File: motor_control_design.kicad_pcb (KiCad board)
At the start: 2 copper layers, 57.1 x 57.2 mm, 97 parts, among them J1 TYPE-C-31-M-12, J10 5V, J2 SWD, J3 VBAT, J4 GND, J5 FC_M/P, J6 Conn_01x06, J7 Conn_01x04_Pin, J8 Conn_01x06, J9 GND, Q1 RF1S9540SM, Q10 2N7002, Q11 2N7002, Q12 2N7002, Q13 2N7002, Q14 RF1S9540SM, Q15 IRLZ44NS, Q16 2N7002, Q2 RF1S9540SM, Q3 IRLZ44NS, Q4 2N7002, Q5 2N7002, Q6 RF1S9540SM, Q7 IRLZ44NS, Q8 2N7002, Q9 IRLZ44NS, U1 STM32F401CCU6, U2 LT1962-3.3, U3 LTC4365DDB, U4 TPS563200, U5 SSM6N7002KFU_LF, Y1 16MHz

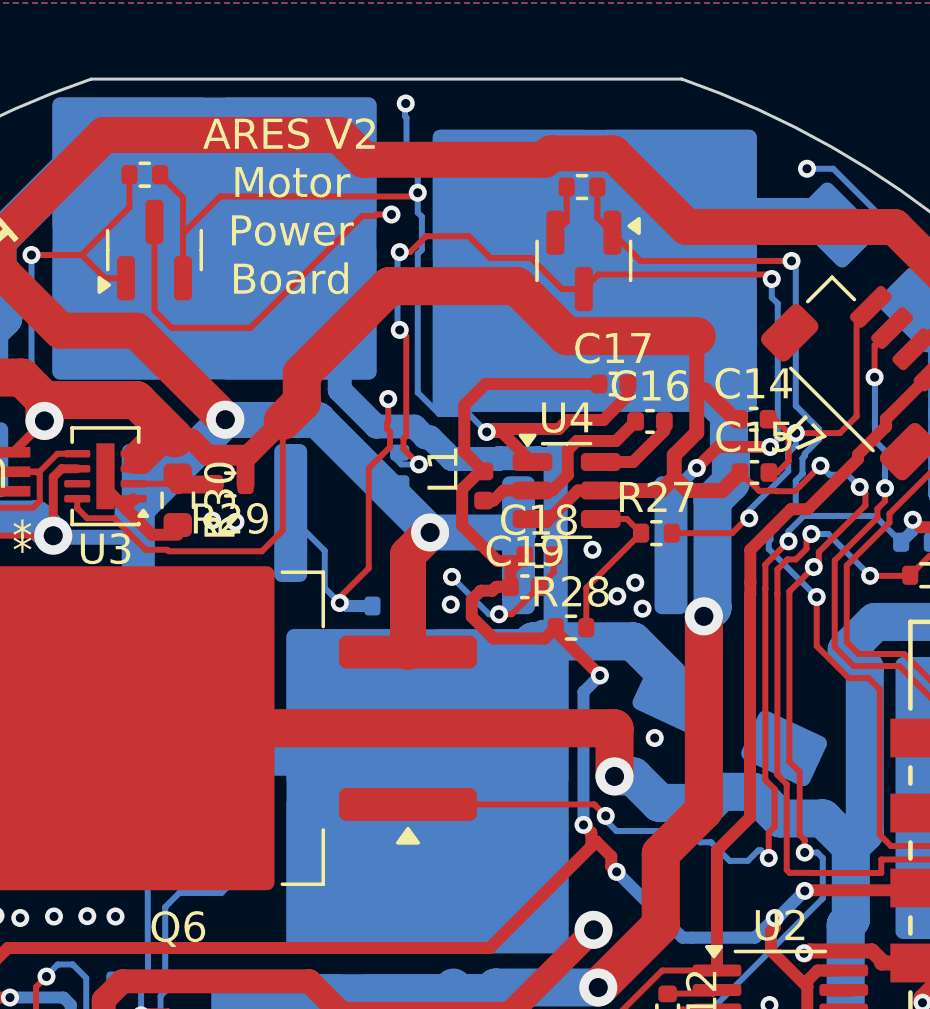
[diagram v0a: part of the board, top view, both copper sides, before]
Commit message: drc: just acceptable board edge errs
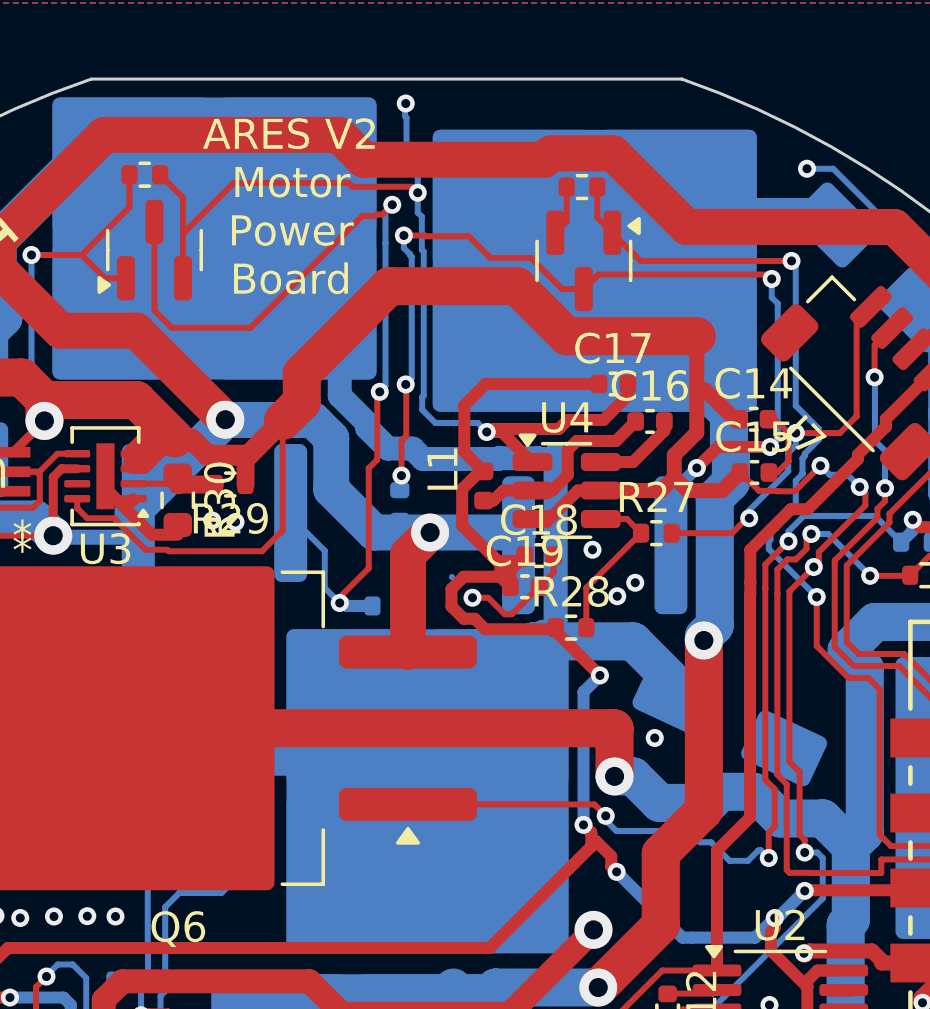
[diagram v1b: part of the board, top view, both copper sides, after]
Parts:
- moved R20 1.25 mm to (149.5, 74.8)
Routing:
- net Net-(Q1-G): track 25.0 -> 31.6 mm
- net +5V: track 116.5 -> 118.7 mm
- net VMOTOR: track 125.4 -> 126.5 mm
- net GND: track 258.3 -> 257.8 mm, vias 136 -> 133

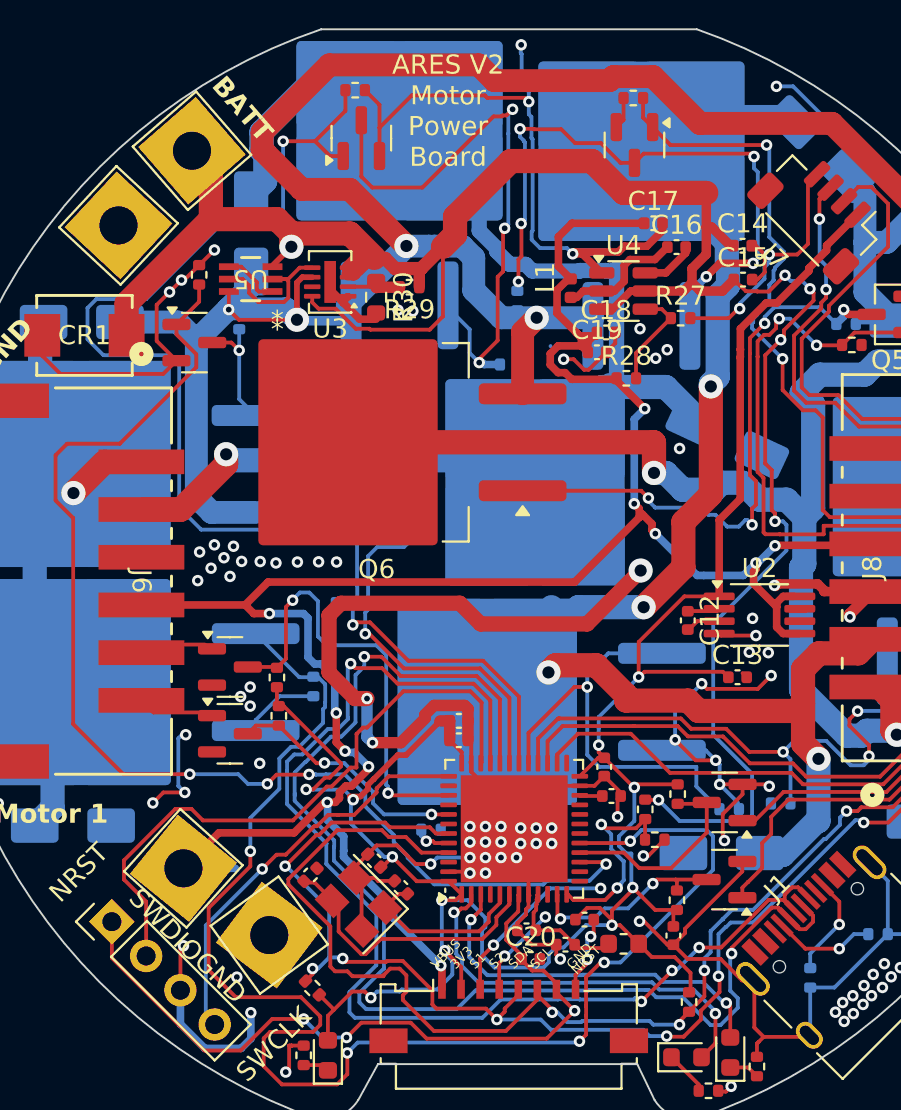
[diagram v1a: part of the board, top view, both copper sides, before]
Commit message: IRF layout 80%
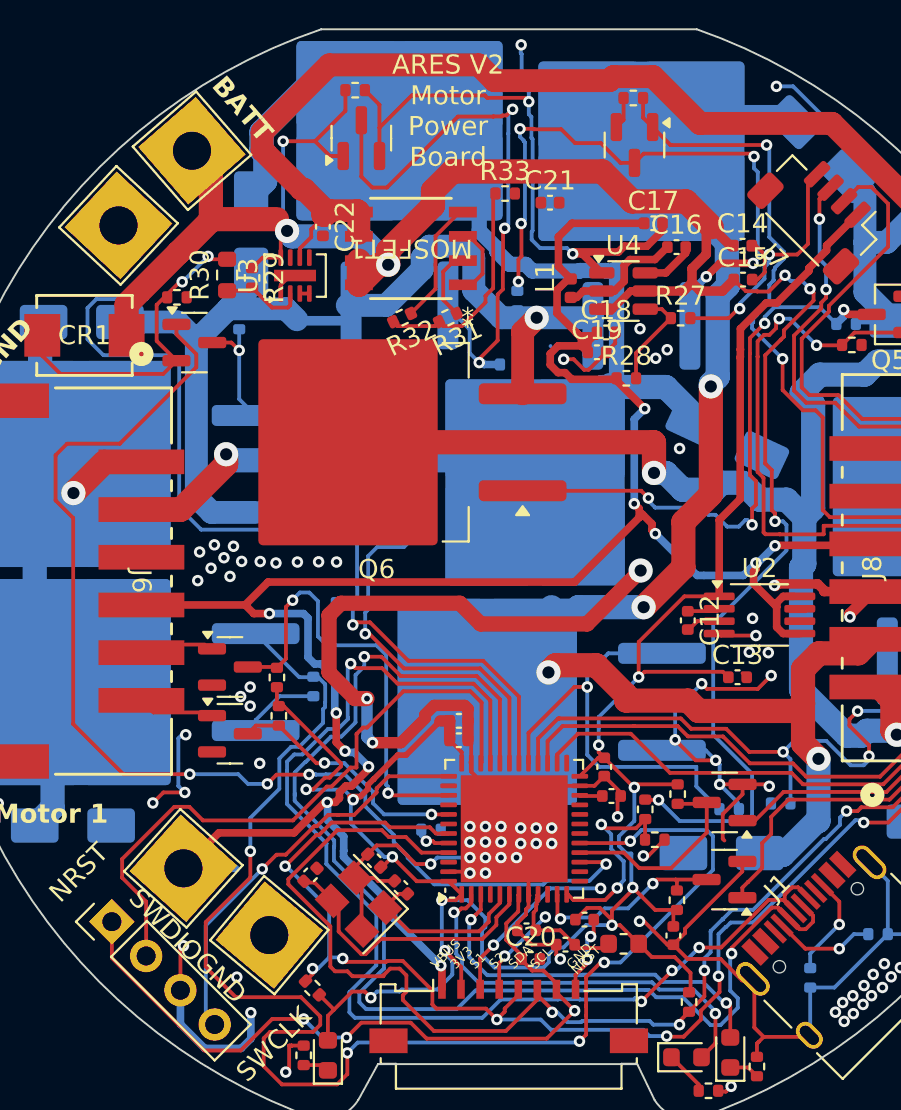
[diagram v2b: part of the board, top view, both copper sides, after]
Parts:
- removed U5: SSM6N7002KFU_LF, CustomARES:SOT-363 US6_TOS-M
- added C21: 3.3nF, Capacitor_SMD:C_0402_1005Metric, F.Cu at (151.2, 69.6)
- added C22: 330uF, Capacitor_SMD:C_0402_1005Metric, F.Cu at (139.3, 70.9)
- added MOSFET1: IRF7351TRPBF, CustomARES:PG-DSO-8-902_INF, F.Cu at (143.9, 72.0)
- added R31: 10k, Resistor_SMD:R_0402_1005Metric, F.Cu at (145.9, 75.6)
- added R32: 10k, Resistor_SMD:R_0402_1005Metric, F.Cu at (143.5, 75.6)
- added R33: 5.1k, Resistor_SMD:R_0402_1005Metric, F.Cu at (148.9, 69.1)
- moved R29 8.26 mm to (135.6, 73.6), turned to -90 degrees
- moved R30 7.90 mm to (134.3, 73.4), turned to 90 degrees
- moved U3 1.87 mm to (137.8, 73.4), turned to 90 degrees
- moved R4 1.66 mm to (131.7, 74.6), turned to 180 degrees
- turned J9 to 50 degrees
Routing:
- net +BATT: track 120.9 -> 107.9 mm
- net Net-(MOSFET1-Pad4): track 0.00 -> 6.54 mm
- net VMOTOR: track 126.5 -> 120.3 mm, vias 5 -> 2
- net Net-(MOSFET1-Pad1): track 0.00 -> 3.86 mm
- net Net-(MOSFET1-Pad2): track 0.00 -> 3.75 mm
- net GND: track 257.8 -> 254.1 mm, vias 133 -> 129
- net Net-(U3-GATE): track 8.01 -> 11.6 mm
- net /SRC: track 3.05 -> 0.00 mm
- net /M1Q1: track 63.3 -> 60.8 mm
- net Net-(U3-OV): track 2.74 -> 4.47 mm

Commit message: OV IC layout done
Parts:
- moved C22 8.91 mm to (144.3, 63.5)
- moved U3 1.36 mm to (138.2, 74.7)
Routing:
- net +BATT: track 107.9 -> 115.9 mm
- net VMOTOR: track 120.3 -> 127.2 mm, vias 2 -> 4
- net Net-(U3-GATE): track 11.6 -> 16.4 mm
- net GND: track 254.1 -> 258.7 mm, vias 129 -> 128
- net Net-(U3-OV): track 4.47 -> 6.25 mm
- net /M1Q1: track 60.8 -> 62.4 mm

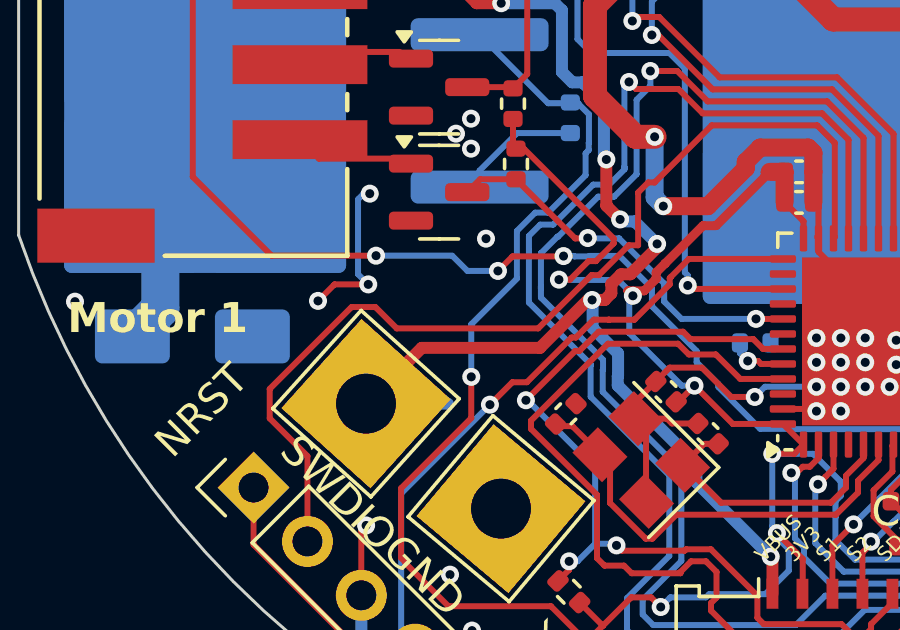
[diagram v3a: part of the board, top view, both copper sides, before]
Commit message: added 5v label on silkscreen
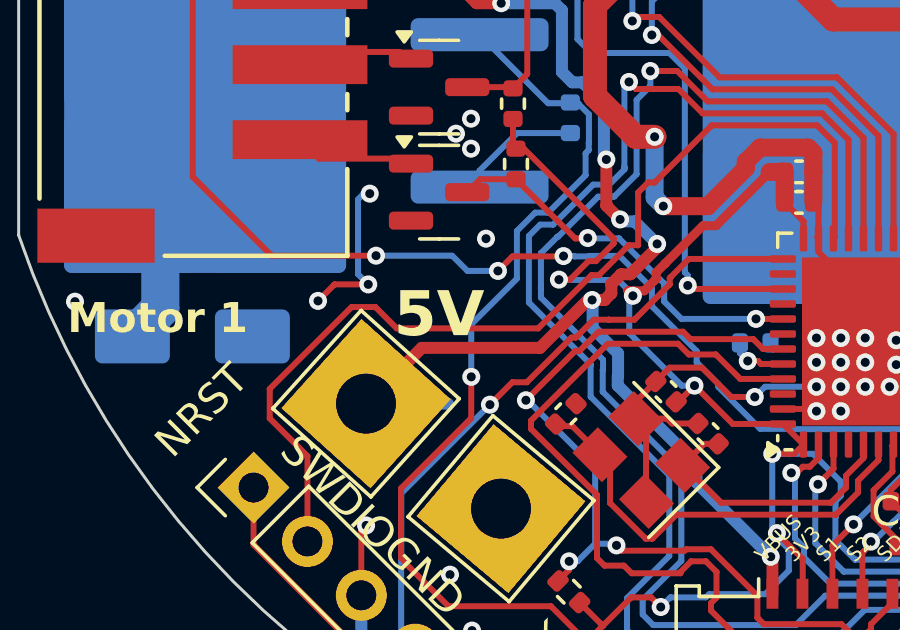
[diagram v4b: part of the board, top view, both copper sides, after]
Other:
- board text added: "5V"
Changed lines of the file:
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@@
+		)
+	)
+	(gr_text "5V\n"
+		(at 132.925 102.4 0)
+		(layer "F.SilkS")
+		(effects
+			(font
+				(size 1.5 1.5)
+				(thickness 0.3)
+				(bold yes)
+			)
+			(justify left bottom)
 		)
 	)

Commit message: original placement
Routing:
- net GND: track 258.7 -> 0.00 mm, vias 128 -> 0
- net +3.3V: track 128.6 -> 0.00 mm, vias 11 -> 0
- net VMOTOR: track 127.2 -> 0.00 mm, vias 4 -> 0
- net +5V: track 118.7 -> 0.00 mm, vias 11 -> 0
- net +BATT: track 115.9 -> 0.00 mm, vias 6 -> 0
- net /SDA: track 103.0 -> 0.00 mm, vias 7 -> 0
- net /SCL: track 97.9 -> 0.00 mm, vias 6 -> 0
- net /M2A: track 80.3 -> 0.00 mm, vias 2 -> 0
- net /M1Q2: track 74.8 -> 0.00 mm, vias 5 -> 0
- net /M1Q3: track 70.5 -> 0.00 mm, vias 2 -> 0
- net /M2B: track 70.2 -> 0.00 mm, vias 4 -> 0
- net /M2Q3: track 69.9 -> 0.00 mm, vias 2 -> 0
- net /USB_D-: track 65.7 -> 0.00 mm, vias 2 -> 0
- net /USB_D+: track 63.4 -> 0.00 mm, vias 4 -> 0
- net /M1Q1: track 62.4 -> 0.00 mm, vias 4 -> 0
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
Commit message: placement in progress
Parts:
- removed J5: FC_M/P, Connector_FFC-FPC:Molex_200528-0080_1x08-1MP_P1.00mm_Horizontal
- Q6: moved to B.Cu
- moved Q14 72.7 mm to (84.1, 57.6)
- moved Q7 72.5 mm to (99.7, 74.8)
- moved Q15 68.0 mm to (84.7, 75.2), turned to 90 degrees
- moved Q3 66.9 mm to (139.8, 150.6), turned to 90 degrees
- moved Q1 63.7 mm to (140.3, 131.0)
- moved Q9 62.5 mm to (156.7, 150.4), turned to 90 degrees
- moved D5 58.4 mm to (117.6, 44.5)
- moved Q2 55.9 mm to (155.7, 131.9), turned to 90 degrees
- moved D12 52.4 mm to (173.4, 53.0)
- moved D9 49.5 mm to (161.0, 53.8)
- moved Q6 49.2 mm to (99.6, 57.4), turned to 90 degrees
- moved R15 37.8 mm to (103.2, 96.5)
- moved R16 37.8 mm to (101.5, 100.9)
- moved D6 35.8 mm to (156.2, 46.4)
- moved R20 30.6 mm to (177.6, 62.5)
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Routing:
- added copper zone on In1.Cu, net GND
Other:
- copper layers 2 -> 4

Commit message: placement 95% done
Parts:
- removed J10: 5V, TestPoint:TestPoint_THTPad_4.0x4.0mm_Drill2.0mm
- removed J9: GND, TestPoint:TestPoint_THTPad_4.0x4.0mm_Drill2.0mm
- added ?: , , F.Cu at (163.7, 103.5)
- added ?: , , F.Cu at (163.7, 74.5)
- added ?: , , F.Cu at (134.7, 74.5)
- added ?: , , F.Cu at (134.7, 103.5)
- D10, D4, D5, D7, D8, R15, R16, R23, R3: moved to F.Cu
- Q13, Q16, Q4, Q5, R17, R24, R4, R6: moved to B.Cu
- moved Q14 87.3 mm to (167.2, 84.2), turned to 0 degrees
- moved Q15 75.7 mm to (152.3, 109.0), turned to 0 degrees
- moved D5 75.3 mm to (148.7, 113.1), turned to 180 degrees
- moved Q7 69.8 mm to (166.3, 95.6), turned to 0 degrees
- moved Q3 65.0 mm to (130.0, 86.2), turned to -90 degrees
- moved Q1 59.3 mm to (141.7, 71.8), turned to -90 degrees
- moved D6 56.5 mm to (130.0, 96.5), turned to -90 degrees
- moved Q6 55.7 mm to (154.0, 69.6), turned to 180 degrees
- moved Q9 55.4 mm to (143.8, 96.5), turned to 180 degrees
- moved D12 53.3 mm to (160.7, 104.8), turned to 90 degrees
- moved R16 52.9 mm to (154.4, 102.5), turned to 0 degrees
- moved Q2 49.8 mm to (142.3, 84.0), turned to 180 degrees
- moved R15 46.5 mm to (149.7, 96.2), turned to 90 degrees
- moved D9 43.6 mm to (175.0, 95.1), turned to 90 degrees
- moved D4 40.8 mm to (149.5, 86.9)
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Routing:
- net GND: track 0.00 -> 9.59 mm, vias 0 -> 1
- net Net-(J8-Pin_6): track 0.00 -> 6.30 mm
- net Net-(J6-Pin_6): track 0.00 -> 6.04 mm
- net +5V: track 0.00 -> 5.68 mm
- net Net-(J6-Pin_5): track 0.00 -> 4.39 mm
- net /E1B: track 0.00 -> 3.75 mm
- net Net-(U4-SW): track 0.00 -> 3.14 mm
- net +BATT: track 0.00 -> 2.67 mm
- net +3.3V: track 0.00 -> 1.63 mm
- net /E1A: track 0.00 -> 1.57 mm
- net Net-(U4-VBST): track 0.00 -> 1.31 mm
- net (no net): vias 0 -> 1

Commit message: routing progress
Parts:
- removed CR1: SMBJ15A, CustomARES:DO-214AASMB_J-BEND_LTF
- added D11: PESD3V3U1UL, Diode_SMD:D_SOD-882, F.Cu at (161.5, 106.2)
- added D13: PESD3V3U1UL, Diode_SMD:D_SOD-882, F.Cu at (162.5, 105.0)
- added D14: PESD3V3U1UL, Diode_SMD:D_SOD-882, F.Cu at (169.5, 73.0)
- added D15: PESD5V0L1UL, Diode_SMD:D_SOD-882, F.Cu at (164.2, 79.3)
- added D16: PESD5V0L1UL, Diode_SMD:D_SOD-882, F.Cu at (164.1, 87.4)
- added D17: PESD5V0L1UL, Diode_SMD:D_SOD-882, F.Cu at (133.2, 98.6)
- added D18: PESD3V3U1UL, Diode_SMD:D_SOD-882, F.Cu at (162.3, 72.3)
- added D19: PESD3V3U1UL, Diode_SMD:D_SOD-882, F.Cu at (161.1, 72.8)
- added D20: PESD5V0L1UL, Diode_SMD:D_SOD-882, F.Cu at (133.5, 90.4)
- added D21: PESD3V3U1UL, Diode_SMD:D_SOD-882, F.Cu at (133.1, 107.5)
- added D22: PESD3V3U1UL, Diode_SMD:D_SOD-882, F.Cu at (132.2, 106.3)
- added D23: PESD3V3U1UL, Diode_SMD:D_SOD-882, F.Cu at (131.1, 105.0)
- moved D5 17.8 mm to (134.8, 102.0)
- moved R12 4.84 mm to (154.9, 107.5), turned to -90 degrees
- moved R11 4.08 mm to (155.4, 105.4)
- moved C20 1.84 mm to (150.9, 108.1)
- moved R15 1.79 mm to (151.1, 95.1)
- moved R23 1.79 mm to (152.2, 95.1)
- moved C10 1.75 mm to (152.3, 108.3)
- moved R21 1.75 mm to (153.9, 107.8)
- moved C11 1.75 mm to (149.9, 110.3)
- moved FB1 1.75 mm to (151.9, 109.8)
- moved C9 1.69 mm to (152.3, 107.0)
- moved Q9 1.68 mm to (142.5, 95.5)
- moved C2 1.43 mm to (143.6, 104.2)
- moved C4 1.43 mm to (146.0, 105.5)
- moved R22 1.43 mm to (156.0, 97.1)
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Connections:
- C14 pad 1: +BATT -> GND
- C14 pad 2: GND -> +BATT
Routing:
- net GND: track 9.59 -> 117.5 mm, vias 1 -> 31
- net +BATT: track 2.67 -> 85.4 mm, vias 0 -> 2
- net /SDA: track 0.00 -> 55.8 mm, vias 0 -> 2
- net /SCL: track 0.00 -> 51.4 mm, vias 0 -> 2
- net +5V: track 5.68 -> 56.4 mm, vias 0 -> 4
- net /M1Q3: track 0.00 -> 44.0 mm, vias 0 -> 1
- net /M2Q1: track 0.00 -> 42.7 mm, vias 0 -> 1
- net /M1Q4: track 0.00 -> 33.9 mm, vias 0 -> 1
- net VMOTOR: track 0.00 -> 31.8 mm, vias 0 -> 12
- net +3.3V: track 1.63 -> 31.1 mm, vias 0 -> 8
- net /NRST: track 0.00 -> 28.6 mm, vias 0 -> 2
- net /M1Q2: track 0.00 -> 27.6 mm, vias 0 -> 1
- net /SWDIO: track 0.00 -> 25.9 mm, vias 0 -> 2
- net /M1Q1: track 0.00 -> 25.5 mm, vias 0 -> 3
- net /SWCLK: track 0.00 -> 22.5 mm, vias 0 -> 2
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- added copper zone on F.Cu, net +3.3V
- added copper zone on In2.Cu, net +3.3V
- added copper zone on F.Cu, net VMOTOR
- added copper zone on In2.Cu, net VMOTOR
